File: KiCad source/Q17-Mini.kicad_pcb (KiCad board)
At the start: 2 copper layers, 95 x 75 mm, 85 parts, among them J1 Input, J2-1 SPK+, J2-2 SPK-, J3-1 V+, J3-2 GND, J3-3 V-, Q1 IRF610, Q10 KSA992, Q11 BS250P, Q12 BD139, Q13 IRF610, Q14 IRF9610, Q15 FQA46N15, Q16 FQA36P15, Q2 KSA992, Q3 KSC1845, Q4 IRF9610, Q5 FQP3P20, Q6 FQP3N30, Q7 KSC1845, Q8 ZVN4206AV, Q9 BS250P, U1 OPA1641, U1' OPA1641

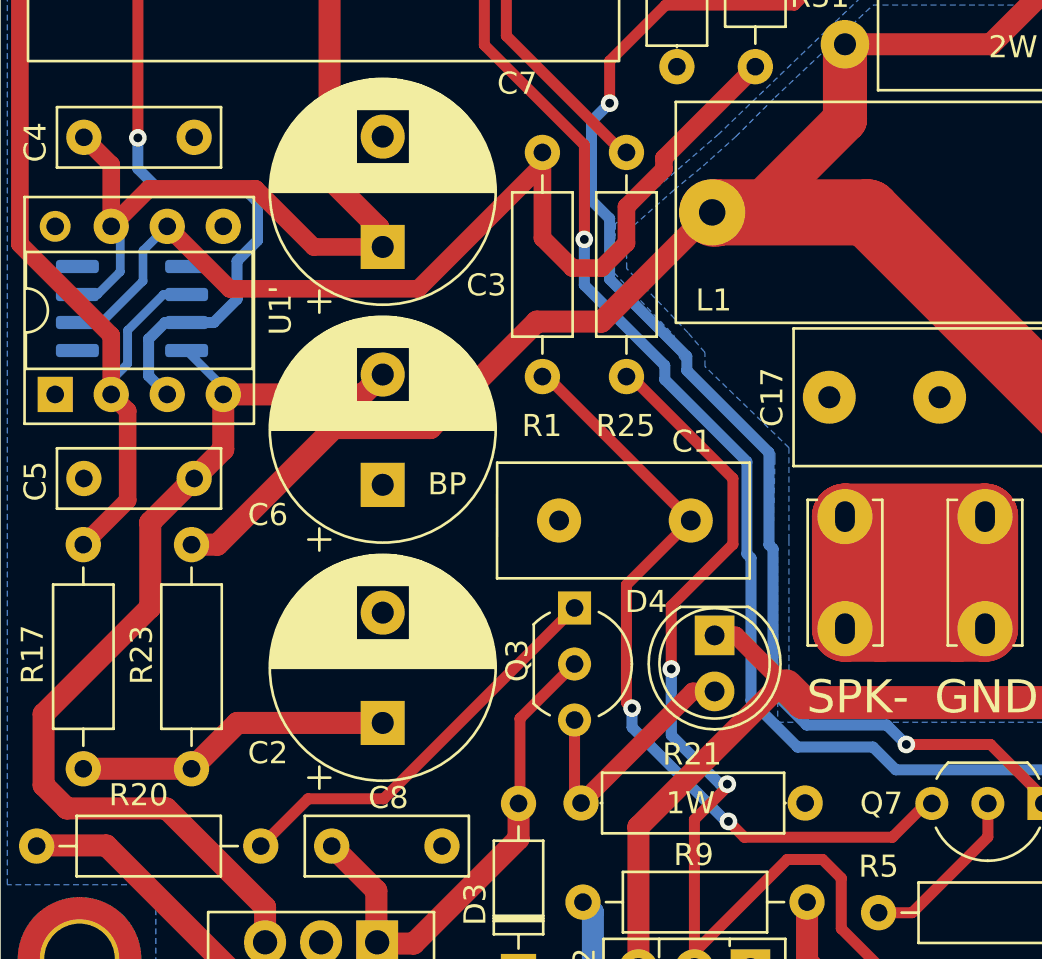
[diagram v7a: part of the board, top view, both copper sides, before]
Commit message: PCB v1.0.8
Move some tracks around D4.
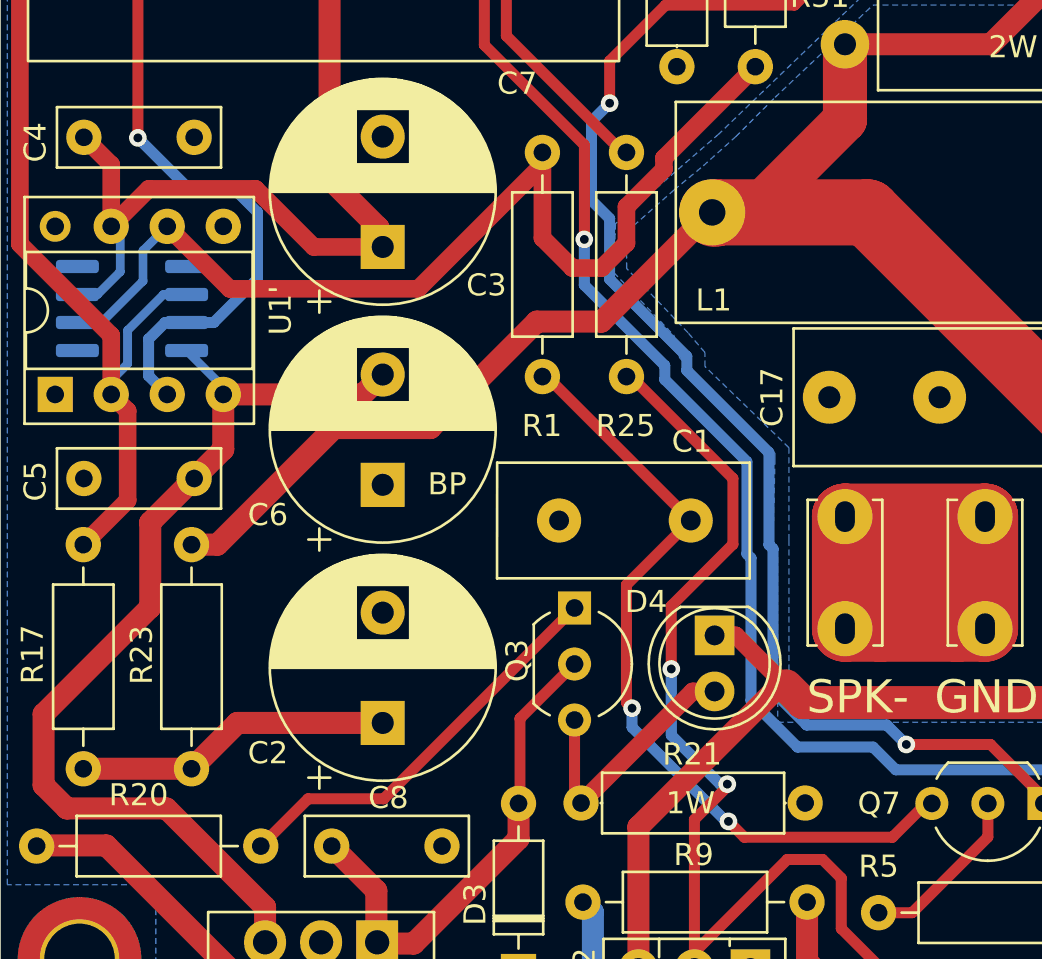
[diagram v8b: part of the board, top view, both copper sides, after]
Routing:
- net Net-(J1-Pad2): track 49.1 -> 48.0 mm
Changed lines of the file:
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@@
     (property "Sheetname" "")
     (attr through_hole)
-    (fp_text reference "Q7" (at 7.366 0) (layer "F.SilkS")
+    (fp_text reference "Q7" (at 7.46919 0) (layer "F.SilkS")
       (effects (font (size 1 1) (thickness 0.15)))
     )
@@
     (effects (font (size 1.5 1.5) (thickness 0.3)) (justify mirror))
   )
-  (gr_text "°" (at 111.379 94.996 -270) (layer "B.SilkS")
+  (gr_text "°" (at 111.420851 94.986062 -270) (layer "B.SilkS")
     (effects (font (size 2 2) (thickness 0.25)))
   )
@@
   (via (at 106.120041 89.205959) (size 0.8) (drill 0.4) (layers "F.Cu" "B.Cu") (net 36))
   (segment (start 106.605197 98.325503) (end 107.352603 97.578097) (width 0.5) (layer "B.Cu") (net 36))
-  (segment (start 111.541511 92.110511) (end 111.099489 91.668489) (width 0.5) (layer "B.Cu") (net 36))
+  (segment (start 108.582571 91.668489) (end 106.120041 89.205959) (width 0.5) (layer "B.Cu") (net 36))
   (segment (start 107.452 100.838) (end 106.605197 99.991197) (width 0.5) (layer "B.Cu") (net 36))
-  (segment (start 110.617 96.52) (end 110.617 94.784341) (width 0.5) (layer "B.Cu") (net 36))
-  (segment (start 109.558903 97.578097) (end 110.617 96.52) (width 0.5) (layer "B.Cu") (net 36))
-  (segment (start 111.099489 91.668489) (end 107.18378 91.668489) (width 0.5) (layer "B.Cu") (net 36))
-  (segment (start 110.617 94.784341) (end 111.541511 93.85983) (width 0.5) (layer "B.Cu") (net 36))
-  (segment (start 111.541511 93.85983) (end 111.541511 92.110511) (width 0.5) (layer "B.Cu") (net 36))
+  (segment (start 110.63383 91.668489) (end 108.582571 91.668489) (width 0.5) (layer "B.Cu") (net 36))
+  (segment (start 111.541511 92.57617) (end 110.63383 91.668489) (width 0.5) (layer "B.Cu") (net 36))
   (segment (start 107.352603 97.578097) (end 108.329717 97.578097) (width 0.5) (layer "B.Cu") (net 36))
+  (segment (start 111.541511 95.595489) (end 111.541511 92.57617) (width 0.5) (layer "B.Cu") (net 36))
   (segment (start 108.329717 97.578097) (end 109.558903 97.578097) (width 0.5) (layer "B.Cu") (net 36))
-  (segment (start 106.120041 90.60475) (end 106.120041 89.205959) (width 0.5) (layer "B.Cu") (net 36))
   (segment (start 106.605197 99.991197) (end 106.605197 98.325503) (width 0.5) (layer "B.Cu") (net 36))
-  (segment (start 107.18378 91.668489) (end 106.120041 90.60475) (width 0.5) (layer "B.Cu") (net 36))
+  (segment (start 109.558903 97.578097) (end 111.541511 95.595489) (width 0.5) (layer "B.Cu") (net 36))
   (segment (start 127.821041 67.00722) (end 127.821041 73.854959) (width 0.5) (layer "F.Cu") (net 37))
   (segment (start 128.110754 89.86722) (end 128.27 89.86722) (width 0.5) (layer "F.Cu") (net 37))
